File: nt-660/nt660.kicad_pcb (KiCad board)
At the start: 2 copper layers, 312 x 96.1 mm, 178 parts, among them J1 USB_mini_micro_B, J2 ISP, K1 KEYSW, K10 KEYSW, K11 KEYSW, K12 KEYSW, K13 KEYSW, K14 KEYSW, K15 KEYSW, K16 KEYSW, K17 KEYSW, K18 KEYSW, K19 KEYSW, K2 KEYSW, K20 KEYSW, K21 KEYSW, K22 KEYSW, K23 KEYSW, K24 KEYSW, K25 KEYSW, K26 KEYSW, K27 KEYSW, K28 KEYSW, K29 KEYSW, K3 KEYSW, K30 KEYSW, K31 KEYSW, K32 KEYSW, K33 KEYSW, K34 KEYSW, K35 KEYSW, K36 KEYSW, K37 KEYSW, K38 KEYSW, K39 KEYSW, K4 KEYSW, K40 KEYSW, K41 KEYSW, K42 KEYSW, K43 KEYSW, K44 KEYSW, K44-1 KEYSW, K46 KEYSW, K46-1 KEYSW, K47 KEYSW, K48 KEYSW, K49 KEYSW, K5 KEYSW, K50 KEYSW, K51 KEYSW, K52 KEYSW, K53 KEYSW, K54 KEYSW, K55 KEYSW, K56 KEYSW, K57 KEYSW, K58 KEYSW, K59 KEYSW, K6 KEYSW, K61 KEYSW, K62 KEYSW, K62-1 KEYSW, K63 KEYSW, K63-1 KEYSW, K67 KEYSW, K67-1 KEYSW, K7 KEYSW, K70 KEYSW, K71 KEYSW, K72 KEYSW, K73 KEYSW, K74 KEYSW, K75 KEYSW, K8 KEYSW, K9 KEYSW, SW1 Reset, U1 ATmega32U4, U2 USBLC6-2SC6, X1 CSTNE16M0V530000R0

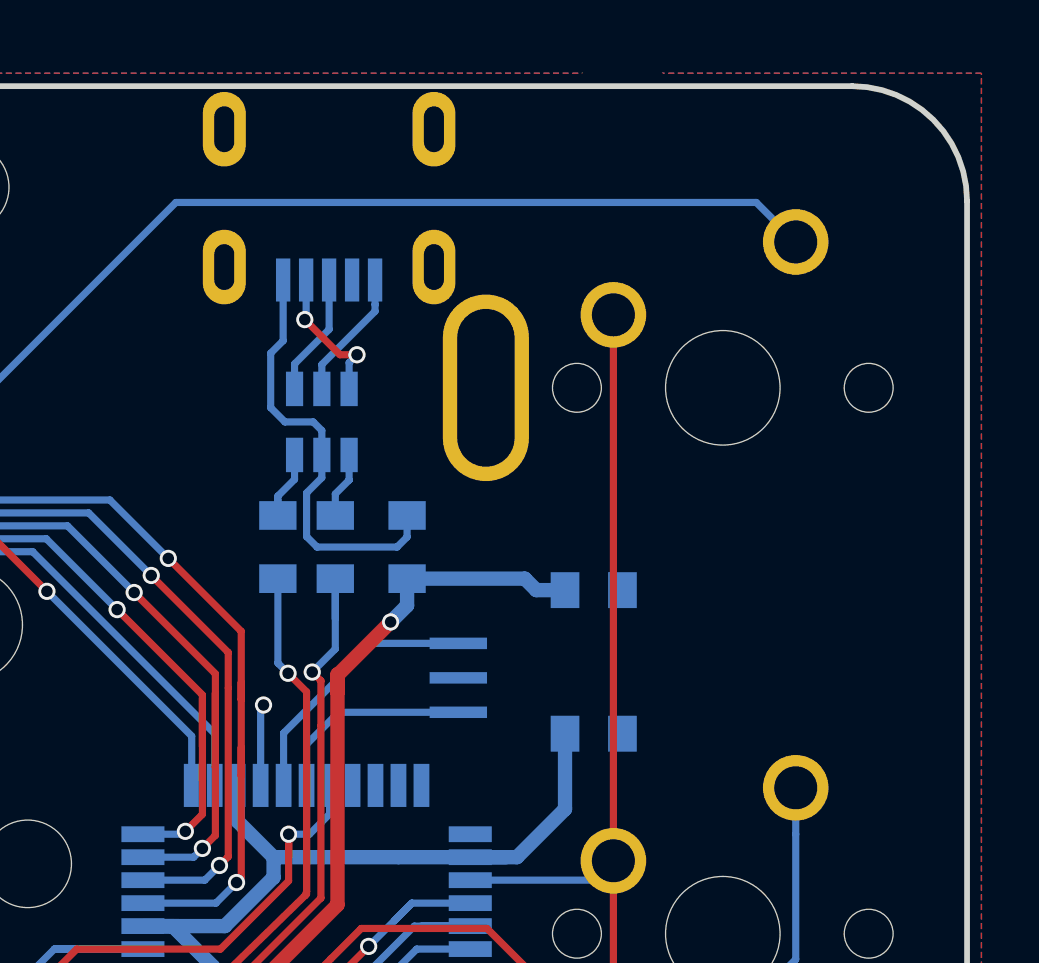
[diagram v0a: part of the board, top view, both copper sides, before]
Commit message: Add rotary encoder and change USB footprint to THT
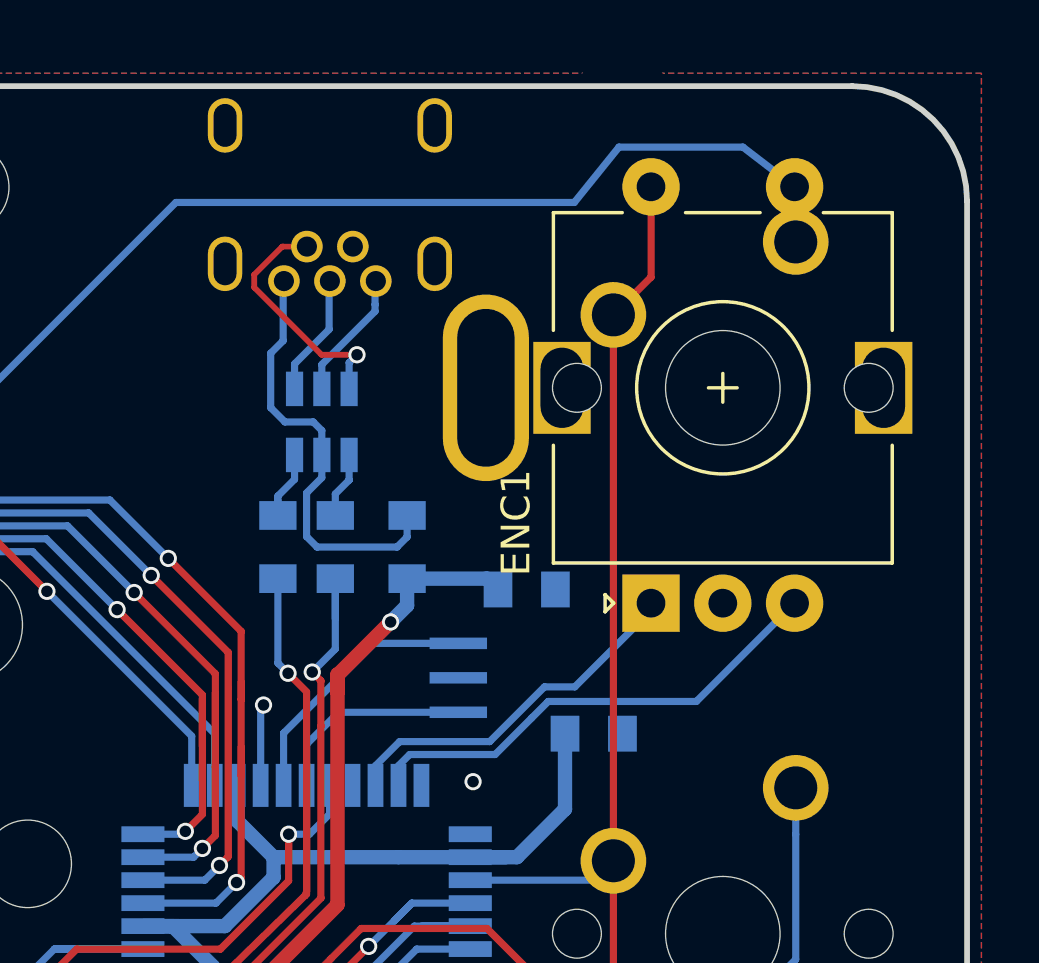
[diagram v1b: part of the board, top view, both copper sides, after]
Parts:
- added ENC1: Rotary_Encoder_Switch, Rotary_Encoder:RotaryEncoder_Alps_EC11E-Switch_Vertical_H20mm, F.Cu at (302.0, 17.0)
- J1: footprint Keeb_components:U-M-M5DD-W-1 -> .github:USB-Mini-B_ LCSC-C46398
- moved J1 4.69 mm to (290.8, 5.19), turned to 0 degrees
- moved C105 2.33 mm to (297.6, 16.5)
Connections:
- J1 pad 4: (no net) -> Net-(J1-Pad4)
- U1 pad 19: (no net) -> Net-(U1-Pad19)
- U1 pad 20: (no net) -> ENCODER_A
- U1 pad 21: (no net) -> ENCODER_B
- U1 pad 22: (no net) -> Net-(U1-Pad22)
- U1 pad 42: (no net) -> Net-(U1-Pad42)
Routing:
- net ENCODER_B: track 0.00 -> 16.8 mm
- net ENCODER_A: track 0.00 -> 12.8 mm
- net col14: track 81.3 -> 86.3 mm
- net D-: track 5.03 -> 8.54 mm, vias 2 -> 1
- net Net-(D15-Pad2): track 33.1 -> 35.8 mm
- net VCC: track 491.4 -> 489.1 mm
- net GND: vias 5 -> 6
